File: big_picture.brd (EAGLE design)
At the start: 160 x 100 mm, 69 parts, among them IC1 LM555N

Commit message: updated big picture
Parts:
- removed ADD1, ADD2, BRAKE, HAZ_L, HAZ_R, HEAD, REAR, WIPER: PSMN039-100YS, nxp_60:SOT669
- removed ADD1_SWITCH, ADD2_SWITCH, BRAKE_SENSOR, DAY_SWITCH, HAZ_L_SWITCH, HAZ_R_SWITCH, WIPER_SWITCH: (no value), switch:M9040P
- removed ADD2_OUT, ADD2_OUT1, ADD2_OUT2, ADD2_OUT3, ADD2_OUT4, ADD2_OUT5, ADD2_OUT6, ADD2_OUT7, VDD_IN: POWERPOLE_POWER25A, powerpoles:POWERPOLE_PAIR_25A
- removed C1: 33uF, rcl:C0805
- removed C10, C8, C9: (no value), rcl:C0805
- removed CONTACT: JJM2W-12V, relay:JJM
- removed D1: (no value), diode:DO34Z7
- removed D2: 1N5817-B, diode:DO41-7.6
- removed HORN: TL36WO, switch:TL3XWO
- removed IC1: LM555N, linear:DIL08
- removed LED1, LED2, LED3, LED4, LED5, LED6, LED7, LED8: (no value), led:CHIP-LED0805
- removed R1, R11, R2, R20, R21, R3, R4, R5, R6: 10K, rcl:R0805
- removed R10: 1K, rcl:R0805
- removed R12, R13, R14, R17, R18, R19, R9: (no value), rcl:R0805
- removed R15, R16: 220, rcl:R0805
- removed R7, R8: 0, rcl:R0805
- removed U$6: HORN, big_picture_parts:HORN
- added DZ1: LZR184, led:LZR184
- added E_STOP1: TL36WO, switch:TL3XWO
- added G1: CR1/2, battery:CR1/2
- added K1: RELAY-SPDT-JZC-11F, SparkFun-Electromechanical:RELAY-JZC
- added M1: MOTOR10MM, SparkFun-Electromechanical:VIBE-MOTOR-10MM
- added S1: TL37PO, switch:TL3XPO
- added SP1: AL30P, buzzer:AL30P
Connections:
- removed net 555_OUT: HAZ_L_SWITCH.2, HAZ_R_SWITCH.2, IC1.3
- removed net GND: ADD1.1, ADD1.2, ADD1.3, ADD2.1, ADD2.2, ADD2.3, BRAKE.1, BRAKE.2, BRAKE.3, C1.2, C10.2, C8.2, C9.2, CONTACT.NO2, D1.A, E_STOP.1, HAZ_L.1, HAZ_L.2, HAZ_L.3, HAZ_R.1, HAZ_R.2, HAZ_R.3, HEAD.1, HEAD.2, HEAD.3, HORN.1, IC1.1, R1.2, R2.2, R20.1, R21.1, R3.2, R4.2, R5.2, R6.2, REAR.1, REAR.2, REAR.3, VDD_IN.BLACK, WIPER.1, WIPER.2, WIPER.3
- removed net H1: BRAKE_SENSOR.1, R17.1
- removed net H2: HAZ_R_SWITCH.1, R16.1
- removed net H3: HAZ_L_SWITCH.1, R15.1
- removed net H4: R14.1, WIPER_SWITCH.1
- removed net H5: ADD1_SWITCH.1, R13.1
- removed net H6: ADD2_SWITCH.1, R12.1
- removed net H7: DAY_SWITCH.1, R18.1, R19.1
- removed net N$10: LED7.C, R21.2
- removed net N$11: LED5.C, R5.1
- removed net N$12: HAZ_R.4, LED5.A, R16.2
- removed net N$13: BRAKE.4, LED6.A, R17.2
- removed net N$14: HEAD.4, LED7.A, R18.2
- removed net N$15: LED8.A, R19.2, REAR.4
- removed net N$16: ADD2_OUT.RED, R7.2
- removed net N$17: ADD1.MB, ADD2_OUT1.BLACK
- removed net N$18: ADD2_OUT1.RED, R8.2
- removed net N$19: ADD2_OUT2.BLACK, D2.A, WIPER.MB
- removed net N$20: ADD2_OUT2.RED, D2.C, R9.2
- removed net N$21: ADD2_OUT3.BLACK, HAZ_L.MB
- removed net N$22: LED3.A, R14.2, WIPER.4
- removed net N$23: ADD2_OUT4.BLACK, HAZ_R.MB
- removed net N$24: HAZ_L.4, LED4.A, R15.2
- removed net N$25: ADD2_OUT5.BLACK, BRAKE.MB
- removed net N$26: ADD1.4, LED2.A, R13.2
- removed net N$27: LED1.C, R1.1
- removed net N$28: LED2.C, R2.1
- removed net N$29: LED4.C, R4.1
- removed net N$30: LED3.C, R3.1
- removed net N$33: LED6.C, R6.1
- removed net N$34: CONTACT.1, CONTACT.C, E_STOP.2, E_STOP.3, U$4.P$2
- removed net N$4: C1.1, IC1.2, IC1.6, R11.2
- removed net N$6: IC1.8, R10.2
- removed net N$8: ADD2.MB, ADD2_OUT.BLACK
- removed net N$9: LED8.C, R20.2
- removed net VDD: ADD1_SWITCH.2, ADD2_OUT3.RED, ADD2_OUT4.RED, ADD2_OUT5.RED, ADD2_OUT6.RED, ADD2_OUT7.RED, ADD2_SWITCH.2, BRAKE_SENSOR.2, CONTACT.2, CONTACT.NO1, DAY_SWITCH.2, VDD_IN.RED, WIPER_SWITCH.2
- removed net VDD_ADD1: C9.1, R8.1
- removed net VDD_ADD2: C8.1, R7.1
- removed net VDD_W: C10.1, D1.C, R9.1
- new net N$35: K1.2, S1.3, U$4.P$1
- net N$1: now also E_STOP1.2, U$4.P$2, U$5.P$2; no longer ADD2_OUT6.BLACK, HEAD.MB
- net N$2: now also G1.-; no longer HORN.2, U$6.P$1
- net N$3: now also E_STOP.2, E_STOP1.1; no longer ADD2_OUT7.BLACK, REAR.MB
- net N$31: now also DZ1.A1, DZ1.A2, DZ1.A3, DZ1.A4, M1.+, SP1.2; no longer HORN.3
- net N$32: now also G1.+, K1.3, S1.2; no longer U$4.P$1, U$5.P$2
- net N$5: now also DZ1.K1, DZ1.K2, DZ1.K3, DZ1.K4, M1.-, SP1.1; no longer IC1.7, R10.1, R11.1
- net N$7: now also E_STOP.1, K1.4; no longer ADD2.4, LED1.A, R12.2

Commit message: added trim pot
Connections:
- net N$5 renamed PDB_GND
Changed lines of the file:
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@@
 <wire x1="-113.03" y1="-82.55" x2="-119.38" y2="-86.36" width="0" layer="19" extent="1-1"/>
 </signal>
-<signal name="N$5">
+<signal name="PDB_GND">
 <contactref element="SP1" pad="1"/>
 <contactref element="M1" pad="-"/>

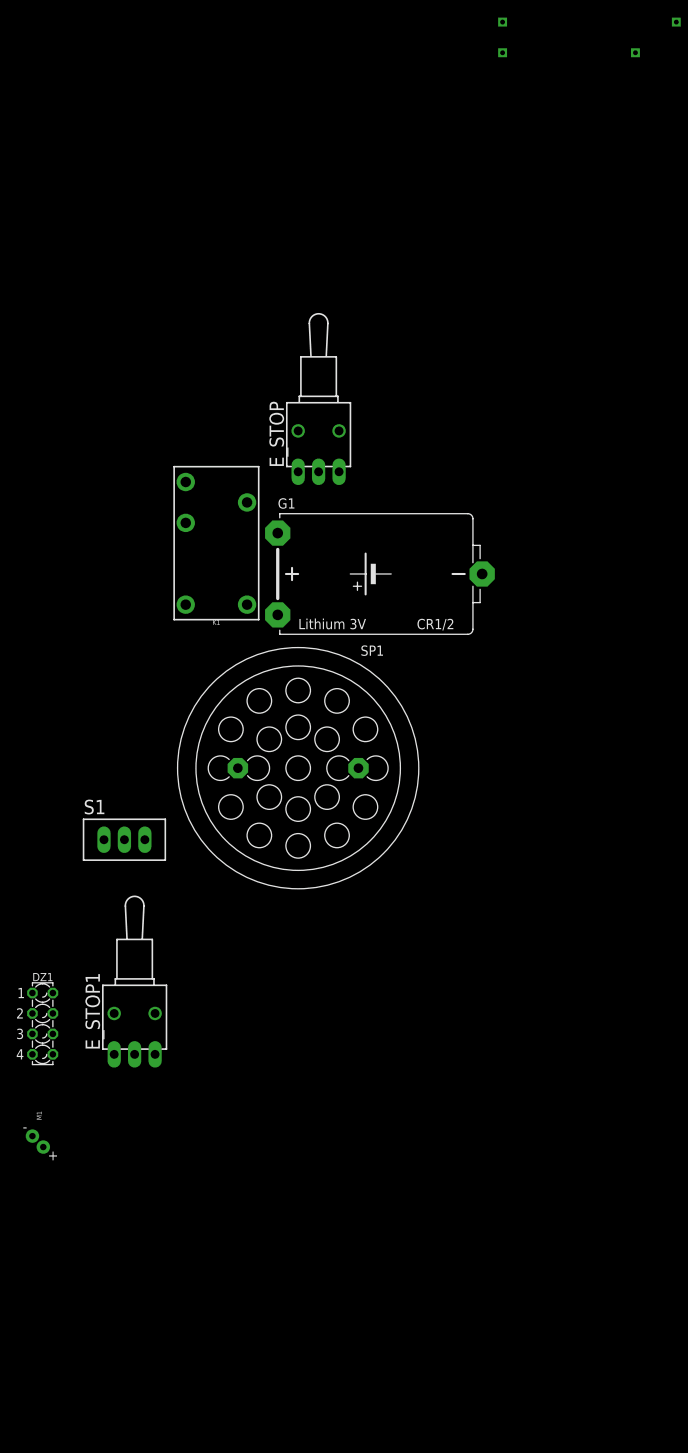
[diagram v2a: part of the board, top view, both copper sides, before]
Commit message: added custom part for buck
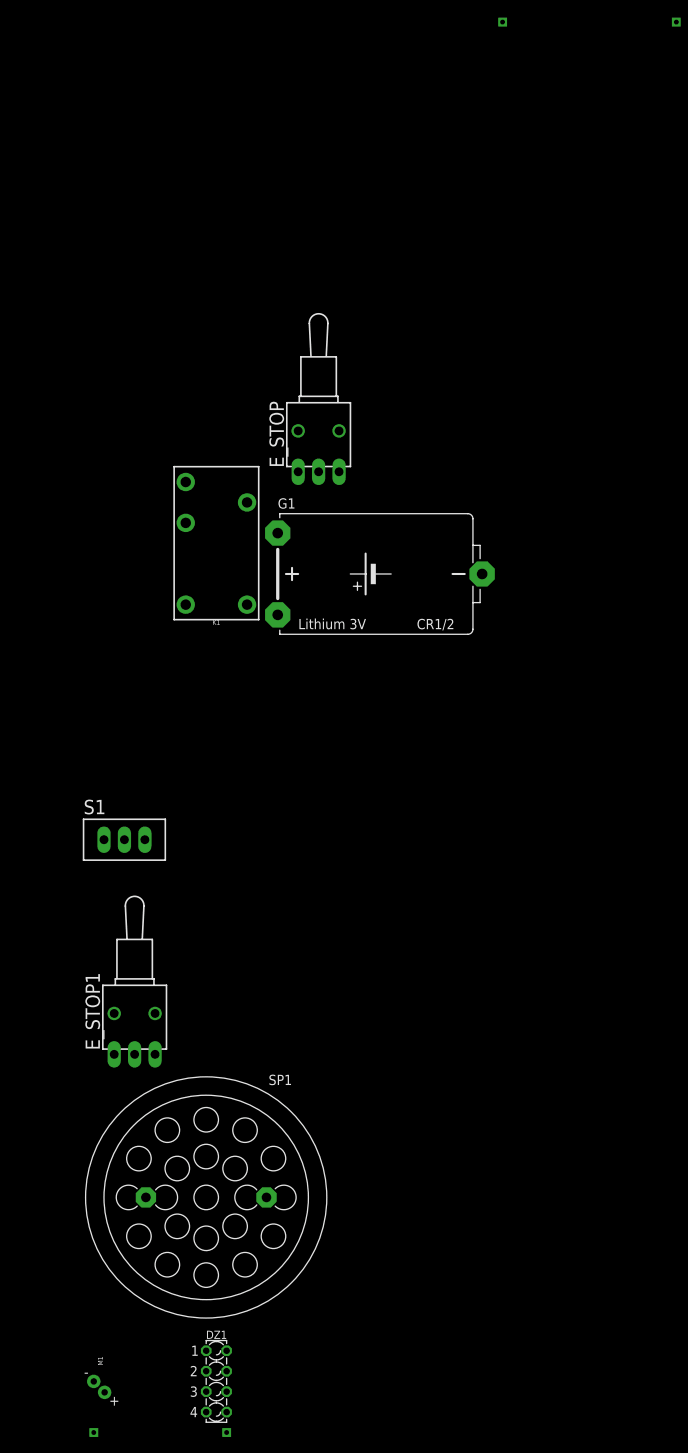
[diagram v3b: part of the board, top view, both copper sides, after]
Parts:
- moved U$5 178.8 mm to (-128.3, -201.9)
- moved SP1 54.6 mm to (-124.5, -172.7)
- moved DZ1 49.4 mm to (-123.2, -195.6)
- moved M1 31.4 mm to (-132.1, -193.0)
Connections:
- new net N$5: U$5.P$2
- net N$1: no longer U$5.P$2
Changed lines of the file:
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@@
 <attribute name="BUCK" value="" x="-74.93" y="-27.94" size="1.778" layer="27" display="off"/>
-</element>
-<element name="U$5" library="big_picture_parts" package="AUX" value="AUX" x="-77.47" y="-30.48">
-<attribute name="AUX" value="" x="-77.47" y="-30.48" size="1.778" layer="27" display="off"/>
 </element>
 <element name="E_STOP" library="switch" library_urn="urn:adsk.eagle:library:380" package="TL3XWO" package3d_urn="urn:adsk.eagle:package:27754/1" value="TL36WO" x="-110.49" y="-77.47">
@@
 <attribute name="SF_SKU" value="COM-00100" x="-123.19" y="-90.17" size="1.778" layer="27" display="off"/>
 </element>
-<element name="SP1" library="buzzer" library_urn="urn:adsk.eagle:library:113" package="AL30P" package3d_urn="urn:adsk.eagle:package:5288/1" value="AL30P" x="-113.03" y="-119.38">
-<attribute name="MF" value="" x="-113.03" y="-119.38" size="1.778" layer="27" display="off"/>
-<attribute name="MPN" value="" x="-113.03" y="-119.38" size="1.778" layer="27" display="off"/>
-<attribute name="OC_FARNELL" value="unknown" x="-113.03" y="-119.38" size="1.778" layer="27" display="off"/>
-<attribute name="OC_NEWARK" value="unknown" x="-113.03" y="-119.38" size="1.778" layer="27" display="off"/>
-</element>
 <element name="S1" library="switch" library_urn="urn:adsk.eagle:library:380" package="TL3XPO" package3d_urn="urn:adsk.eagle:package:27745/1" value="TL37PO" x="-134.62" y="-128.27"/>
 <element name="E_STOP1" library="switch" library_urn="urn:adsk.eagle:library:380" package="TL3XWO" package3d_urn="urn:adsk.eagle:package:27754/1" value="TL36WO" x="-133.35" y="-149.86"/>
-<element name="DZ1" library="led" library_urn="urn:adsk.eagle:library:259" package="LZR184" package3d_urn="urn:adsk.eagle:package:15790/1" value="LZR184" x="-144.78" y="-151.13"/>
-<element name="M1" library="SparkFun-Electromechanical" library_urn="urn:adsk.eagle:library:516" package="VIBE-MOTOR-10MM" package3d_urn="urn:adsk.eagle:package:38555/1" value="MOTOR10MM" x="-139.7" y="-162.56">
-<attribute name="PROD_ID" value="COMP-08572" x="-139.7" y="-162.56" size="1.778" layer="27" display="off"/>
-<attribute name="SF_SKU" value="ROB-08449" x="-139.7" y="-162.56" size="1.778" layer="27" display="off"/>
+<element name="U$5" library="big_picture_parts" package="AUX" value="AUX" x="-128.27" y="-201.93">
+<attribute name="AUX" value="" x="-128.27" y="-157.48" size="1.778" layer="27" display="off"/>
+</element>
+<element name="SP1" library="buzzer" library_urn="urn:adsk.eagle:library:113" package="AL30P" package3d_urn="urn:adsk.eagle:package:5288/1" value="AL30P" x="-124.46" y="-172.72">
+<attribute name="MF" value="" x="-124.46" y="-175.26" size="1.778" layer="27" display="off"/>
+<attribute name="MPN" value="" x="-124.46" y="-175.26" size="1.778" layer="27" display="off"/>
+<attribute name="OC_FARNELL" value="unknown" x="-124.46" y="-175.26" size="1.778" layer="27" display="off"/>
+<attribute name="OC_NEWARK" value="unknown" x="-124.46" y="-175.26" size="1.778" layer="27" display="off"/>
+</element>
+<element name="DZ1" library="led" library_urn="urn:adsk.eagle:library:259" package="LZR184" package3d_urn="urn:adsk.eagle:package:15790/1" value="LZR184" x="-123.19" y="-195.58"/>
+<element name="M1" library="SparkFun-Electromechanical" library_urn="urn:adsk.eagle:library:516" package="VIBE-MOTOR-10MM" package3d_urn="urn:adsk.eagle:package:38555/1" value="MOTOR10MM" x="-132.08" y="-193.04">
+<attribute name="PROD_ID" value="COMP-08572" x="-139.7" y="-195.58" size="1.778" layer="27" display="off"/>
+<attribute name="SF_SKU" value="ROB-08449" x="-139.7" y="-195.58" size="1.778" layer="27" display="off"/>
 </element>
 </elements>
 <signals>
-<signal name="N$31">
-<contactref element="U$5" pad="P$1"/>
-<contactref element="SP1" pad="2"/>
-<contactref element="M1" pad="+"/>
-<contactref element="DZ1" pad="A1"/>
-<contactref element="DZ1" pad="A2"/>
-<contactref element="DZ1" pad="A4"/>
-<contactref element="DZ1" pad="A3"/>
-<wire x1="-146.05" y1="-147.32" x2="-105.537" y2="-119.38" width="0" layer="19" extent="1-1"/>
-<wire x1="-146.05" y1="-149.86" x2="-146.05" y2="-147.32" width="0" layer="19" extent="1-1"/>
-<wire x1="-146.05" y1="-152.4" x2="-146.05" y2="-149.86" width="0" layer="19" extent="1-1"/>
-<wire x1="-146.05" y1="-154.94" x2="-146.05" y2="-152.4" width="0" layer="19" extent="1-1"/>
-<wire x1="-144.7" y1="-166.46" x2="-146.05" y2="-154.94" width="0" layer="19" extent="1-1"/>
-<wire x1="-87.63" y1="-30.48" x2="-105.537" y2="-119.38" width="0" layer="19" extent="1-1"/>
-</signal>
 <signal name="N$32">
 <contactref element="G1" pad="+"/>
@@
 <contactref element="U$4" pad="P$2"/>
 <contactref element="E_STOP1" pad="2"/>
-<contactref element="U$5" pad="P$2"/>
-<wire x1="-66.04" y1="-26.67" x2="-71.12" y2="-30.48" width="0" layer="19" extent="1-1"/>
-<wire x1="-133.35" y1="-154.94" x2="-71.12" y2="-30.48" width="0" layer="19" extent="1-1"/>
+<wire x1="-133.35" y1="-154.94" x2="-66.04" y2="-26.67" width="0" layer="19" extent="1-1"/>
 </signal>
 <signal name="N$3">
@@
 <wire x1="-113.03" y1="-82.55" x2="-119.38" y2="-86.36" width="0" layer="19" extent="1-1"/>
 </signal>
+<signal name="N$2">
+<contactref element="G1" pad="-"/>
+</signal>
+<signal name="N$31">
+<contactref element="U$5" pad="P$1"/>
+<contactref element="SP1" pad="2"/>
+<contactref element="M1" pad="+"/>
+<contactref element="DZ1" pad="A1"/>
+<contactref element="DZ1" pad="A2"/>
+<contactref element="DZ1" pad="A4"/>
+<contactref element="DZ1" pad="A3"/>
+<wire x1="-137.08" y1="-196.94" x2="-138.43" y2="-201.93" width="0" layer="19" extent="1-1"/>
+<wire x1="-124.46" y1="-196.85" x2="-137.08" y2="-196.94" width="0" layer="19" extent="1-1"/>
+<wire x1="-124.46" y1="-199.39" x2="-124.46" y2="-196.85" width="0" layer="19" extent="1-1"/>
+<wire x1="-124.46" y1="-194.31" x2="-124.46" y2="-196.85" width="0" layer="19" extent="1-1"/>
+<wire x1="-124.46" y1="-191.77" x2="-124.46" y2="-194.31" width="0" layer="19" extent="1-1"/>
+<wire x1="-116.967" y1="-172.72" x2="-124.46" y2="-191.77" width="0" layer="19" extent="1-1"/>
+</signal>
+<signal name="N$5">
+<contactref element="U$5" pad="P$2"/>
+</signal>
 <signal name="PDB_GND">
 <contactref element="SP1" pad="1"/>
@@
 <contactref element="DZ1" pad="K3"/>
 <contactref element="DZ1" pad="K4"/>
-<wire x1="-143.51" y1="-147.32" x2="-120.523" y2="-119.38" width="0" layer="19" extent="1-1"/>
-<wire x1="-143.51" y1="-149.86" x2="-143.51" y2="-147.32" width="0" layer="19" extent="1-1"/>
-<wire x1="-143.51" y1="-152.4" x2="-143.51" y2="-149.86" width="0" layer="19" extent="1-1"/>
-<wire x1="-143.51" y1="-154.94" x2="-143.51" y2="-152.4" width="0" layer="19" extent="1-1"/>
-<wire x1="-146.05" y1="-165.1" x2="-143.51" y2="-154.94" width="0" layer="19" extent="1-1"/>
-</signal>
-<signal name="N$2">
-<contactref element="G1" pad="-"/>
+<wire x1="-121.92" y1="-196.85" x2="-138.43" y2="-195.58" width="0" layer="19" extent="1-1"/>
+<wire x1="-121.92" y1="-199.39" x2="-121.92" y2="-196.85" width="0" layer="19" extent="1-1"/>
+<wire x1="-121.92" y1="-194.31" x2="-121.92" y2="-196.85" width="0" layer="19" extent="1-1"/>
+<wire x1="-121.92" y1="-191.77" x2="-121.92" y2="-194.31" width="0" layer="19" extent="1-1"/>
+<wire x1="-131.953" y1="-172.72" x2="-121.92" y2="-191.77" width="0" layer="19" extent="1-1"/>
 </signal>
 </signals>

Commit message: redid general schematic
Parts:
- removed U$4: BUCK, big_picture_parts:BUCK
- removed U$5: AUX, big_picture_parts:AUX
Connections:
- new net N$2: DZ1.A1
- new net N$8: DZ1.A3
- new net N$9: DZ1.A2
- net N$1: no longer U$4.P$2
- net N$31: no longer DZ1.A1, DZ1.A2, DZ1.A3, DZ1.A4, M1.+, U$5.P$1
- net N$35: no longer U$4.P$1
- net N$5: now also M1.+; no longer U$5.P$2
- net PDB_GND: no longer DZ1.K4
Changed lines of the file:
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@@
 <element name="U$2" library="big_picture_parts" package="BUCK" value="" x="-8.89" y="-24.13"/>
 <element name="U$3" library="big_picture_parts" package="HORN" value="" x="0" y="-34.29"/>
-<element name="U$4" library="big_picture_parts" package="BUCK" value="BUCK" x="-74.93" y="-27.94">
-<attribute name="BUCK" value="" x="-74.93" y="-27.94" size="1.778" layer="27" display="off"/>
-</element>
 <element name="E_STOP" library="switch" library_urn="urn:adsk.eagle:library:380" package="TL3XWO" package3d_urn="urn:adsk.eagle:package:27754/1" value="TL36WO" x="-110.49" y="-77.47">
 <attribute name="NAME" x="-114.808" y="-82.042" size="1.778" layer="25" rot="R90"/>
@@
 <element name="S1" library="switch" library_urn="urn:adsk.eagle:library:380" package="TL3XPO" package3d_urn="urn:adsk.eagle:package:27745/1" value="TL37PO" x="-134.62" y="-128.27"/>
 <element name="E_STOP1" library="switch" library_urn="urn:adsk.eagle:library:380" package="TL3XWO" package3d_urn="urn:adsk.eagle:package:27754/1" value="TL36WO" x="-133.35" y="-149.86"/>
-<element name="U$5" library="big_picture_parts" package="AUX" value="AUX" x="-128.27" y="-201.93">
-<attribute name="AUX" value="" x="-128.27" y="-157.48" size="1.778" layer="27" display="off"/>
-</element>
 <element name="SP1" library="buzzer" library_urn="urn:adsk.eagle:library:113" package="AL30P" package3d_urn="urn:adsk.eagle:package:5288/1" value="AL30P" x="-124.46" y="-172.72">
 <attribute name="MF" value="" x="-124.46" y="-175.26" size="1.778" layer="27" display="off"/>
@@
 <contactref element="K1" pad="2"/>
 <contactref element="S1" pad="3"/>
-<contactref element="U$4" pad="P$1"/>
 <wire x1="-132.08" y1="-128.27" x2="-127" y2="-88.9" width="0" layer="19" extent="1-1"/>
-<wire x1="-87.63" y1="-26.67" x2="-127" y2="-88.9" width="0" layer="19" extent="1-1"/>
 </signal>
 <signal name="N$1">
-<contactref element="U$4" pad="P$2"/>
 <contactref element="E_STOP1" pad="2"/>
-<wire x1="-133.35" y1="-154.94" x2="-66.04" y2="-26.67" width="0" layer="19" extent="1-1"/>
 </signal>
 <signal name="N$3">
@@
 <wire x1="-113.03" y1="-82.55" x2="-119.38" y2="-86.36" width="0" layer="19" extent="1-1"/>
 </signal>
-<signal name="N$2">
-<contactref element="G1" pad="-"/>
-</signal>
 <signal name="N$31">
-<contactref element="U$5" pad="P$1"/>
 <contactref element="SP1" pad="2"/>
-<contactref element="M1" pad="+"/>
-<contactref element="DZ1" pad="A1"/>
-<contactref element="DZ1" pad="A2"/>
-<contactref element="DZ1" pad="A4"/>
-<contactref element="DZ1" pad="A3"/>
-<wire x1="-137.08" y1="-196.94" x2="-138.43" y2="-201.93" width="0" layer="19" extent="1-1"/>
-<wire x1="-124.46" y1="-196.85" x2="-137.08" y2="-196.94" width="0" layer="19" extent="1-1"/>
-<wire x1="-124.46" y1="-199.39" x2="-124.46" y2="-196.85" width="0" layer="19" extent="1-1"/>
-<wire x1="-124.46" y1="-194.31" x2="-124.46" y2="-196.85" width="0" layer="19" extent="1-1"/>
-<wire x1="-124.46" y1="-191.77" x2="-124.46" y2="-194.31" width="0" layer="19" extent="1-1"/>
-<wire x1="-116.967" y1="-172.72" x2="-124.46" y2="-191.77" width="0" layer="19" extent="1-1"/>
-</signal>
-<signal name="N$5">
-<contactref element="U$5" pad="P$2"/>
 </signal>
 <signal name="PDB_GND">
@@
 <contactref element="DZ1" pad="K2"/>
 <contactref element="DZ1" pad="K3"/>
-<contactref element="DZ1" pad="K4"/>
 <wire x1="-121.92" y1="-196.85" x2="-138.43" y2="-195.58" width="0" layer="19" extent="1-1"/>
-<wire x1="-121.92" y1="-199.39" x2="-121.92" y2="-196.85" width="0" layer="19" extent="1-1"/>
 <wire x1="-121.92" y1="-194.31" x2="-121.92" y2="-196.85" width="0" layer="19" extent="1-1"/>
 <wire x1="-121.92" y1="-191.77" x2="-121.92" y2="-194.31" width="0" layer="19" extent="1-1"/>
 <wire x1="-131.953" y1="-172.72" x2="-121.92" y2="-191.77" width="0" layer="19" extent="1-1"/>
 </signal>
+<signal name="N$4">
+<contactref element="G1" pad="-"/>
+</signal>
+<signal name="N$2">
+<contactref element="DZ1" pad="A1"/>
+</signal>
+<signal name="N$5">
+<contactref element="M1" pad="+"/>
+</signal>
+<signal name="N$8">
+<contactref element="DZ1" pad="A3"/>
+</signal>
+<signal name="N$9">
+<contactref element="DZ1" pad="A2"/>
+</signal>
 </signals>
